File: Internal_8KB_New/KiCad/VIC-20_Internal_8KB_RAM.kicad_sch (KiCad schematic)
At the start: 11 parts, among them J1 RAM Decoder, J2 UD4, J3 UE4, U1 74HCT04, U2 74HCT138, U3 62256, U4 74HCT30

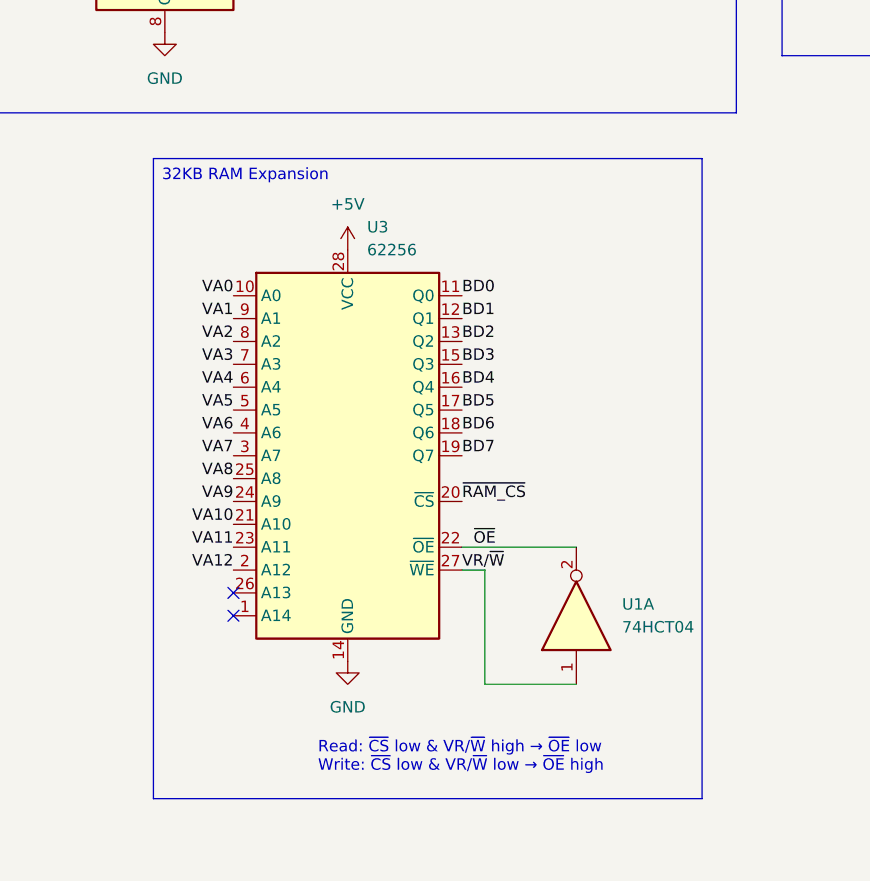
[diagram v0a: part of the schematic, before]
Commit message: Swapped 62256 -> 6264
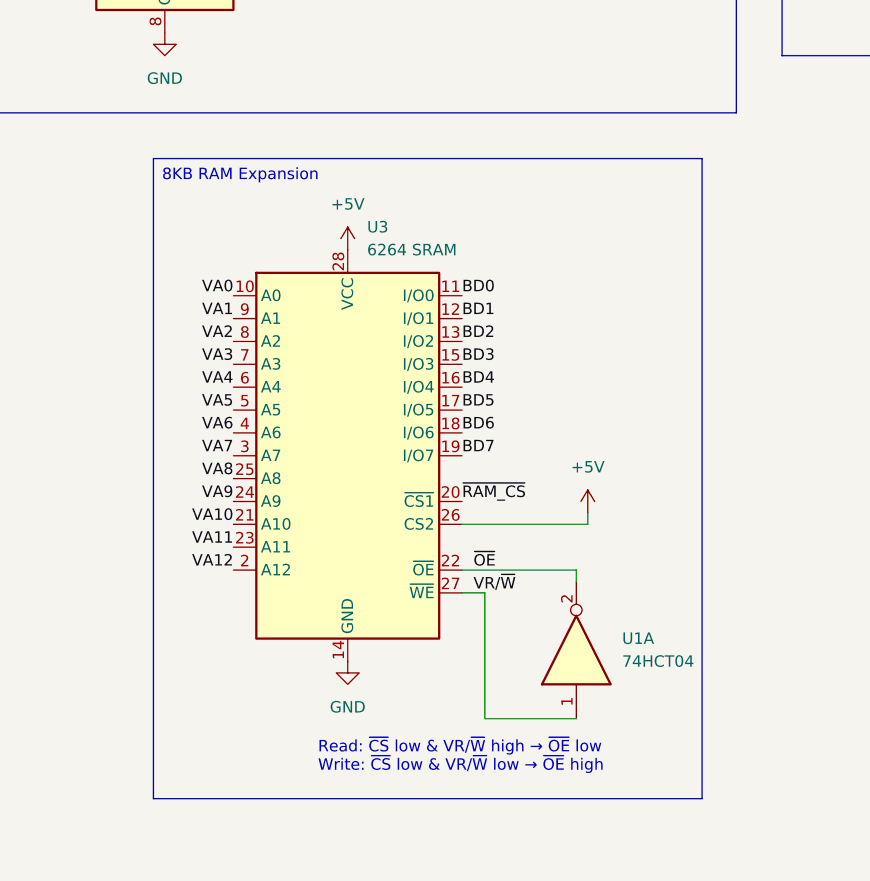
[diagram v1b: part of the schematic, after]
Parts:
- removed U3: 62256, Package_DIP:DIP-28_W15.24mm, symbol Memory_RAM:HM62256BLP
- added U3: 6264 SRAM, Package_DIP:DIP-28_W15.24mm, symbol Memory_RAM:HY6264AxP
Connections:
- net +5V: now also U3.26 (CS2), U3.28 (VCC)
- net BD0: now also U3.11 (I/O0)
- net BD1: now also U3.12 (I/O1)
- net BD2: now also U3.13 (I/O2)
- net BD3: now also U3.15 (I/O3)
- net BD4: now also U3.16 (I/O4)
- net BD5: now also U3.17 (I/O5)
- net BD6: now also U3.18 (I/O6)
- net BD7: now also U3.19 (I/O7)
- net GND: now also U3.14 (GND)
- net VA0: now also U3.10 (A0)
- net VA1: now also U3.9 (A1)
- net VA10: now also U3.21 (A10)
- net VA11: now also U3.23 (A11)
- net VA12: now also U3.2 (A12)
- net VA2: now also U3.8 (A2)
- net VA3: now also U3.7 (A3)
- net VA4: now also U3.6 (A4)
- net VA5: now also U3.5 (A5)
- net VA6: now also U3.4 (A6)
- net VA7: now also U3.3 (A7)
- net VA8: now also U3.25 (A8)
- net VA9: now also U3.24 (A9)
- net VR/~{W}: now also U3.27 (~{WE})
- net ~{OE}: now also U3.22 (~{OE})
- net ~{RAM_CS}: now also U3.20 (~{CS1})
- no-connect marks 29 -> 27
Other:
- moved on the sheet: U1A

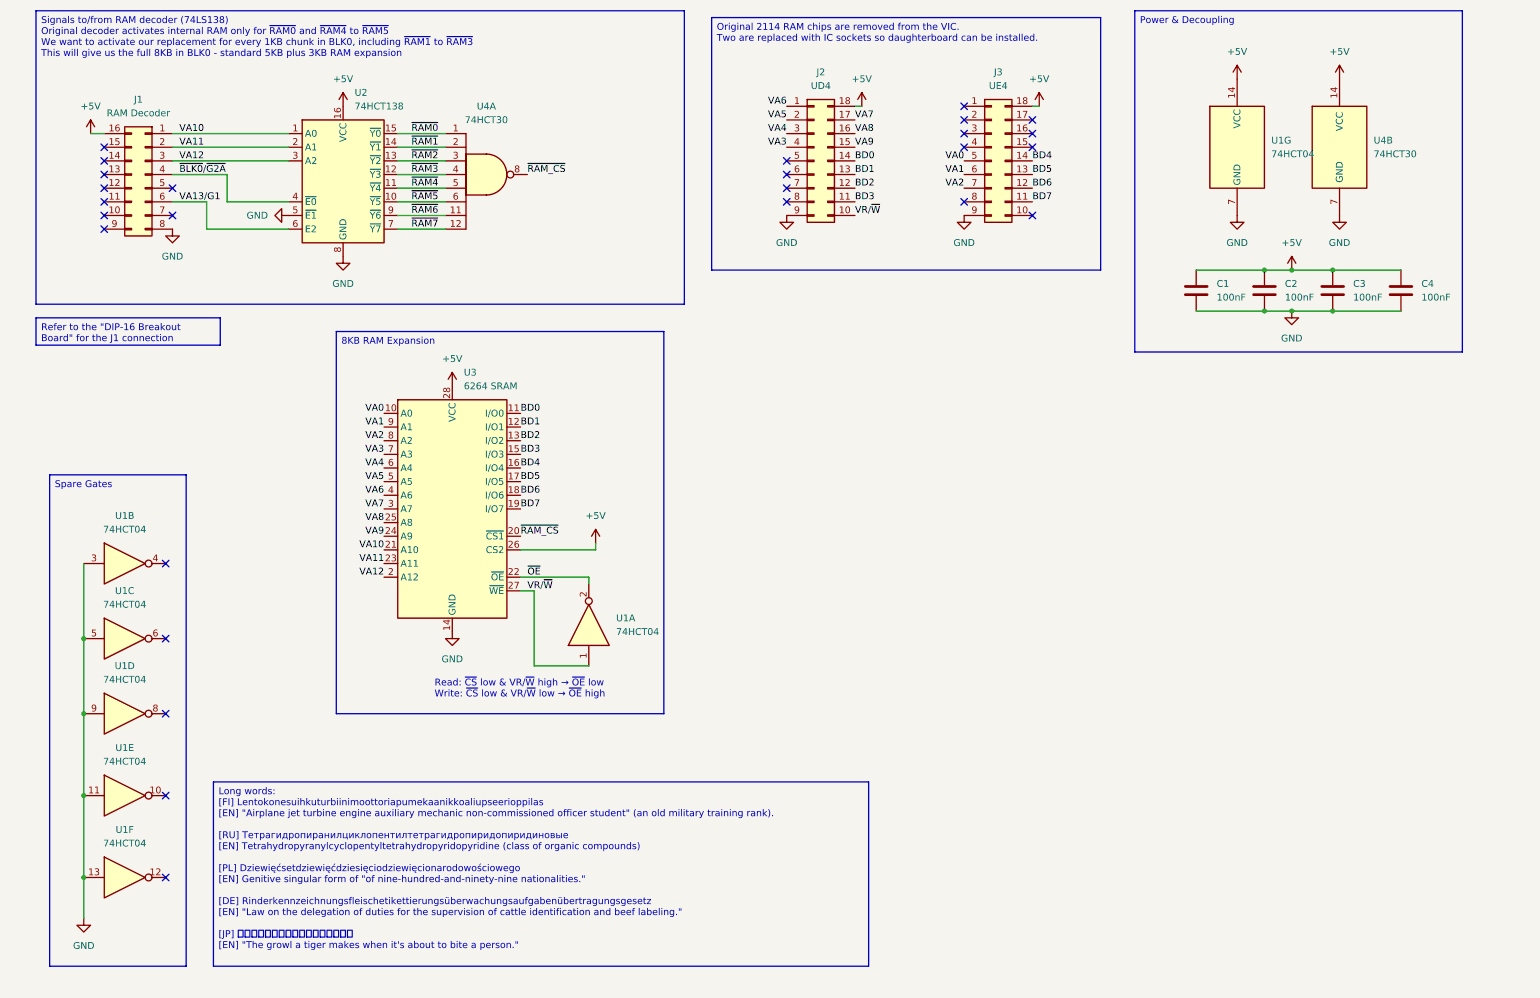
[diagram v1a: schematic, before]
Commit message: Revised BLK0 expansion
Added enable/disable function to return VIC to unexpanded 5KB state
~RAM1/~RAM2/~RAM3 select signals routed back to VIC when disabled
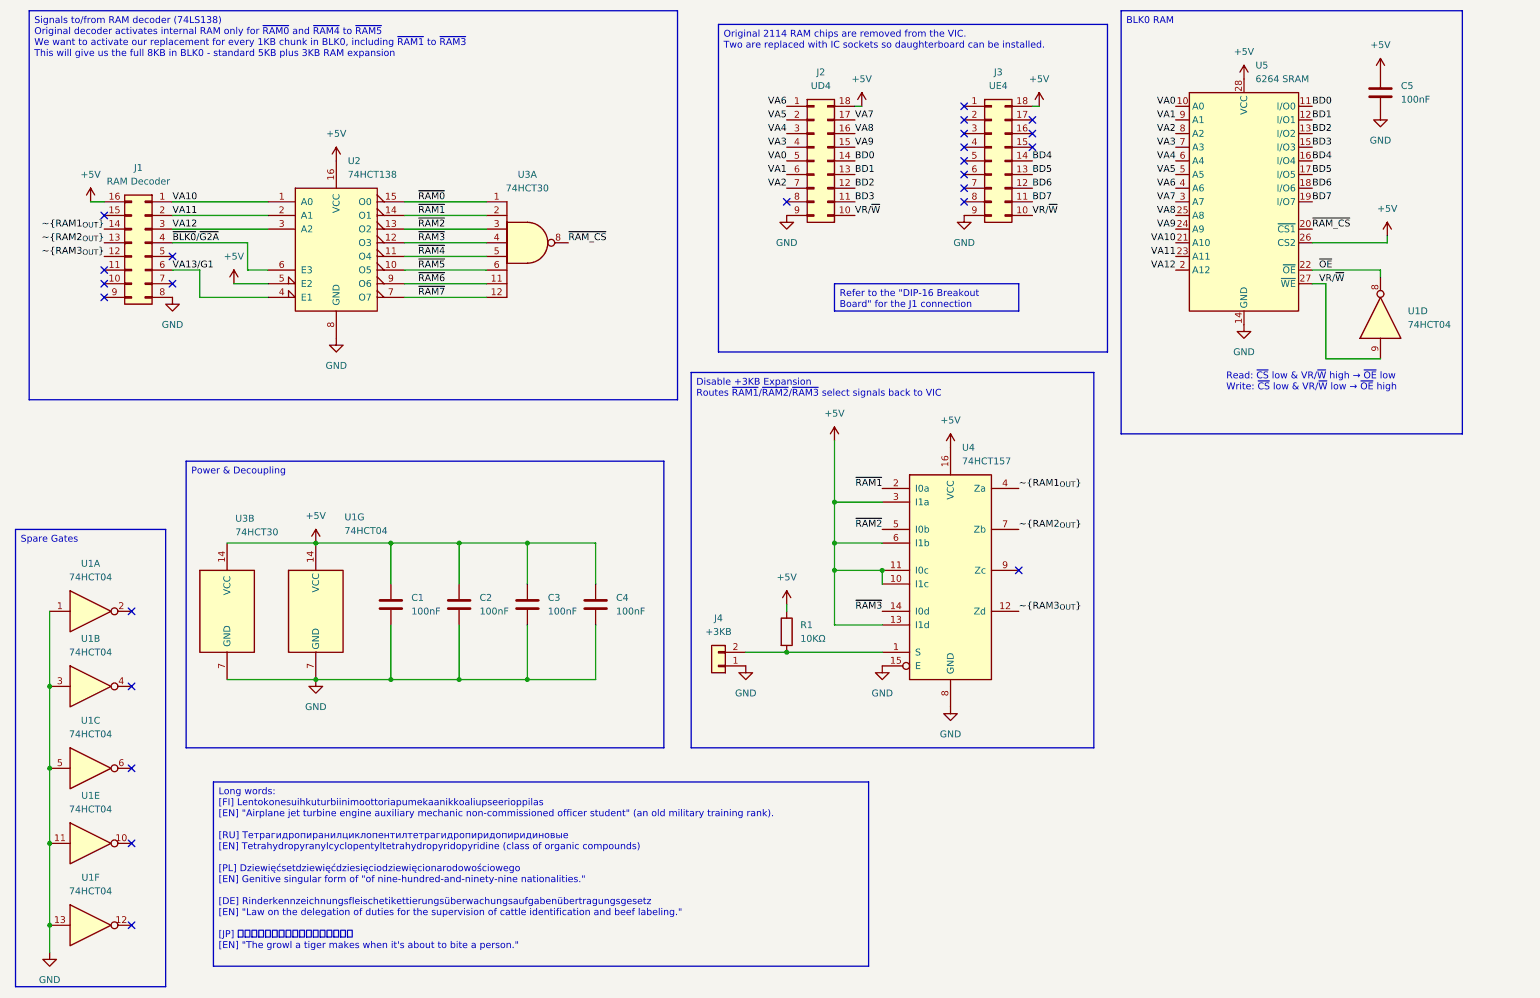
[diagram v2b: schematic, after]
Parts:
- removed U1: 74HCT04, Package_DIP:DIP-14_W7.62mm, symbol 74xx:74LS04
- removed U2: 74HCT138, Package_DIP:DIP-16_W7.62mm, symbol 74xx:74HCT138
- removed U4: 74HCT30, Package_DIP:DIP-14_W7.62mm, symbol 74xx:74LS30
- added C5: 100nF, Capacitor_THT:C_Disc_D3.0mm_W2.0mm_P2.50mm, symbol Device:C
- added J4: +3KB, Connector_PinHeader_2.54mm:PinHeader_1x02_P2.54mm_Vertical, symbol Connector_Generic:Conn_01x02
- added R1: 10KΩ, Resistor_THT:R_Axial_DIN0207_L6.3mm_D2.5mm_P7.62mm_Horizontal, symbol Device:R
- added U1: 74HCT04, Package_DIP:DIP-14_W7.62mm, symbol 74xx:74HCT04
- added U2: 74HCT138, Package_DIP:DIP-16_W7.62mm, symbol 74xx:74LS138
- added U3: 74HCT30, Package_DIP:DIP-14_W7.62mm, symbol 74xx:74LS30
- added U4: 74HCT157, Package_DIP:DIP-16_W7.62mm, symbol 74xx:74LS157
- renumbered U3 to U5
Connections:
- net +5V: now also C5.1, R1.1, U1.14 (VCC), U2.16 (VCC), U2.5 (E2), U3.14 (VCC), U4.10 (I1c), U4.11 (I0c), U4.13 (I1d), U4.16 (VCC), U4.3 (I1a), U4.6 (I1b)
- net GND: now also C5.2, J4.1 (Pin_1), U1.1, U1.11, U1.13, U1.3, U1.5, U1.7 (GND), U2.8 (GND), U3.7 (GND), U4.15 (E), U4.8 (GND)
- net VA0: now also J2.5 (Pin_5); no longer J3.5 (Pin_5)
- net VA1: now also J2.6 (Pin_6); no longer J3.6 (Pin_6)
- net VA10: now also U2.1 (A0)
- net VA11: now also U2.2 (A1)
- net VA12: now also U2.3 (A2)
- net VA13/G1: now also U2.4 (E1)
- net VA2: now also J2.7 (Pin_7); no longer J3.7 (Pin_7)
- net VR/~{W}: now also J3.10 (Pin_10), U1.9
- net ~{BLK0}/~{G2A}: now also U2.6 (E3)
- net ~{OE}: now also U1.8
- net ~{RAM0}: now also U2.15 (O0), U3.1
- net ~{RAM1}: now also U2.14 (O1), U3.2, U4.2 (I0a)
- net ~{RAM2}: now also U2.13 (O2), U3.3, U4.5 (I0b)
- net ~{RAM3}: now also U2.12 (O3), U3.4, U4.14 (I0d)
- net ~{RAM4}: now also U2.11 (O4), U3.5
- net ~{RAM5}: now also U2.10 (O5), U3.6
- net ~{RAM6}: now also U2.9 (O6), U3.11
- net ~{RAM7}: now also U2.7 (O7), U3.12
- net ~{RAM_CS}: now also U3.8
- net ~{RAM3_{OUT}}: now reaches J1.12 (Pin_12)
- net ~{RAM3_{OUT}}: now also U4.12 (Zd)
- net ~{RAM2_{OUT}}: now reaches J1.13 (Pin_13)
- net ~{RAM2_{OUT}}: now also U4.7 (Zb)
- net ~{RAM1_{OUT}}: now reaches J1.14 (Pin_14)
- net ~{RAM1_{OUT}}: now also U4.4 (Za)
- new net: J4.2 (Pin_2), R1.2, U4.1 (S)
- no-connect marks 27 -> 24
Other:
- moved on the sheet: C1, C2, J1, U5
